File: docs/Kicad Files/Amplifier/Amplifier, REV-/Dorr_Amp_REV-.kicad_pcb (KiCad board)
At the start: 2 copper layers, 152.7 x 76.2 mm, 48 parts, among them J1 Speaker Terminals, J2 Input Terminals, J3 Power Input, Q1 2N3904, Q10 QD44H8G, Q2 QD45H8G, Q3 2N3904, Q4 2N3906, Q5 QD44H8G, Q6 2N3904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

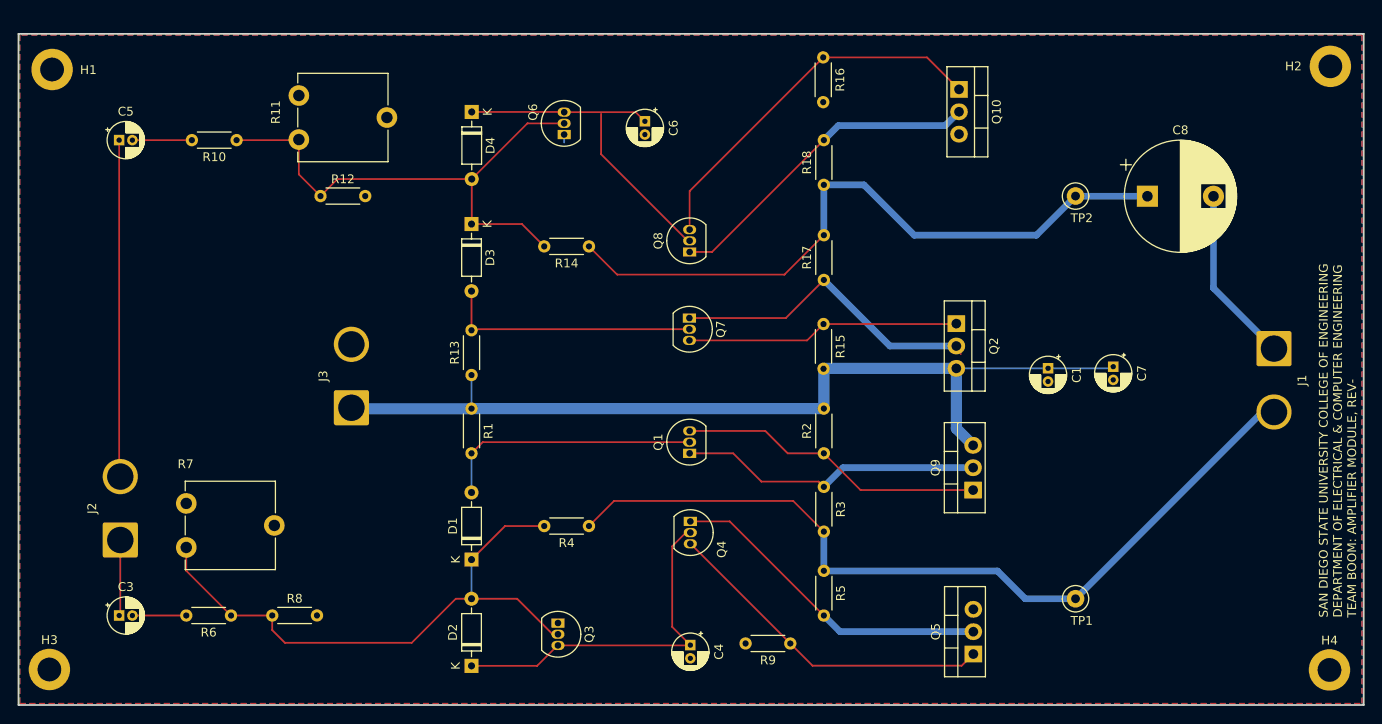
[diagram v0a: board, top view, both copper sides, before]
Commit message: Fixed all footprints
All footprints should be good. Need to double check the capacitor lead spacing with those in the lab.
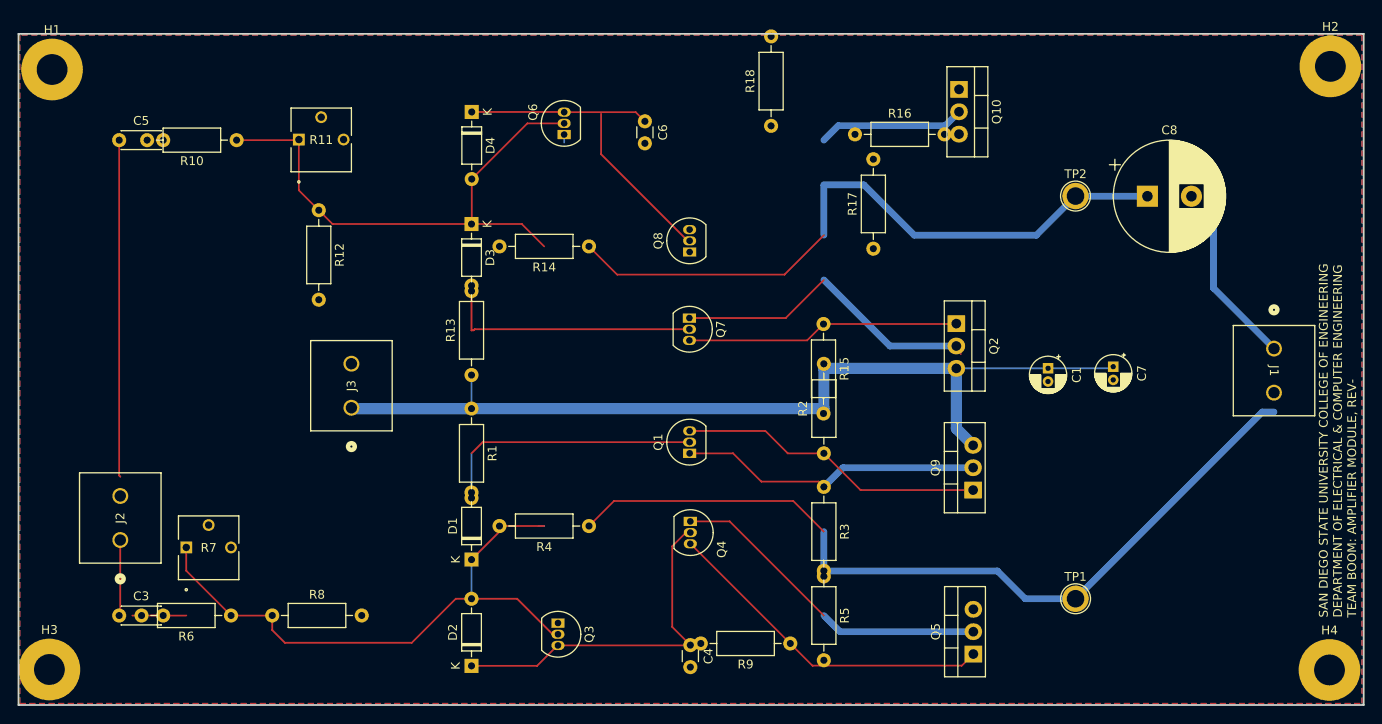
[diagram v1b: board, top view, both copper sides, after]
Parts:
- C3, C5: footprint Capacitor_THT:CP_Radial_D4.0mm_P1.50mm -> Capacitor_THT:C_Disc_D4.3mm_W1.9mm_P5.00mm
- C4, C6: footprint Capacitor_THT:CP_Radial_D4.0mm_P1.50mm -> Capacitor_THT:C_Disc_D3.0mm_W1.6mm_P2.50mm
- C8: footprint Capacitor_THT:CP_Radial_D12.5mm_P7.50mm -> Capacitor_THT:CP_Radial_D12.5mm_P5.00mm
- H1, H2, H3, H4: footprint MountingHole:MountingHole_2.7mm_M2.5_DIN965_Pad -> MountingHole:MountingHole_3.5mm_Pad
- J1: value Speaker Terminals -> Speaker; footprint Connector_Wire:SolderWire-2.5sqmm_1x02_P7.2mm_D2.4mm_OD3.6mm -> Z_Custom_Footprints:CONN_1935776_PXC
- J2, J3: footprint Connector_Wire:SolderWire-2.5sqmm_1x02_P7.2mm_D2.4mm_OD3.6mm -> Z_Custom_Footprints:CONN_1935776_PXC
- R1, R10, R12, R13, R14, R15, R16, R17, R18, R2, R3, R4, R5, R6, R8, R9: footprint Resistor_THT:R_Axial_DIN0204_L3.6mm_D1.6mm_P5.08mm_Horizontal -> Resistor_THT:R_Axial_DIN0207_L6.3mm_D2.5mm_P10.16mm_Horizontal
- R11, R7: footprint Potentiometer_THT:Potentiometer_ACP_CA9-V10_Vertical -> Z_Custom_Footprints:POT_3362P
- TP1, TP2: footprint TestPoint:TestPoint_Loop_D2.50mm_Drill1.0mm -> TestPoint:TestPoint_Plated_Hole_D2.0mm
- moved R16 9.45 mm to (133.4, 74.0), turned to 0 degrees
- moved R18 8.99 mm to (123.9, 73.1)
- moved R17 6.65 mm to (135.5, 87.0)
- moved R12 1.62 mm to (72.5, 82.7), turned to -90 degrees
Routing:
- net Net-(Q10-B): track 42.8 -> 0.00 mm
- net Net-(Q10-C): track 37.2 -> 16.7 mm
- net Net-(C5-Pad2): track 6.76 -> 0.00 mm
- net Net-(D3-K): track 60.1 -> 61.7 mm

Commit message: All footprints verified
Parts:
- C1, C7: footprint Capacitor_THT:CP_Radial_D4.0mm_P1.50mm -> Capacitor_THT:C_Rect_L7.0mm_W3.5mm_P5.00mm
- C3, C5: footprint Capacitor_THT:C_Disc_D4.3mm_W1.9mm_P5.00mm -> Capacitor_THT:CP_Radial_D5.0mm_P2.00mm
- C4, C6: footprint Capacitor_THT:C_Disc_D3.0mm_W1.6mm_P2.50mm -> Capacitor_THT:C_Disc_D5.1mm_W3.2mm_P5.00mm
- J1, J2, J3: footprint Z_Custom_Footprints:CONN_1935776_PXC -> Custom_Footprints:CONN_1935776_PXC
- R11, R7: footprint Z_Custom_Footprints:POT_3362P -> Custom_Footprints:POT_3362P

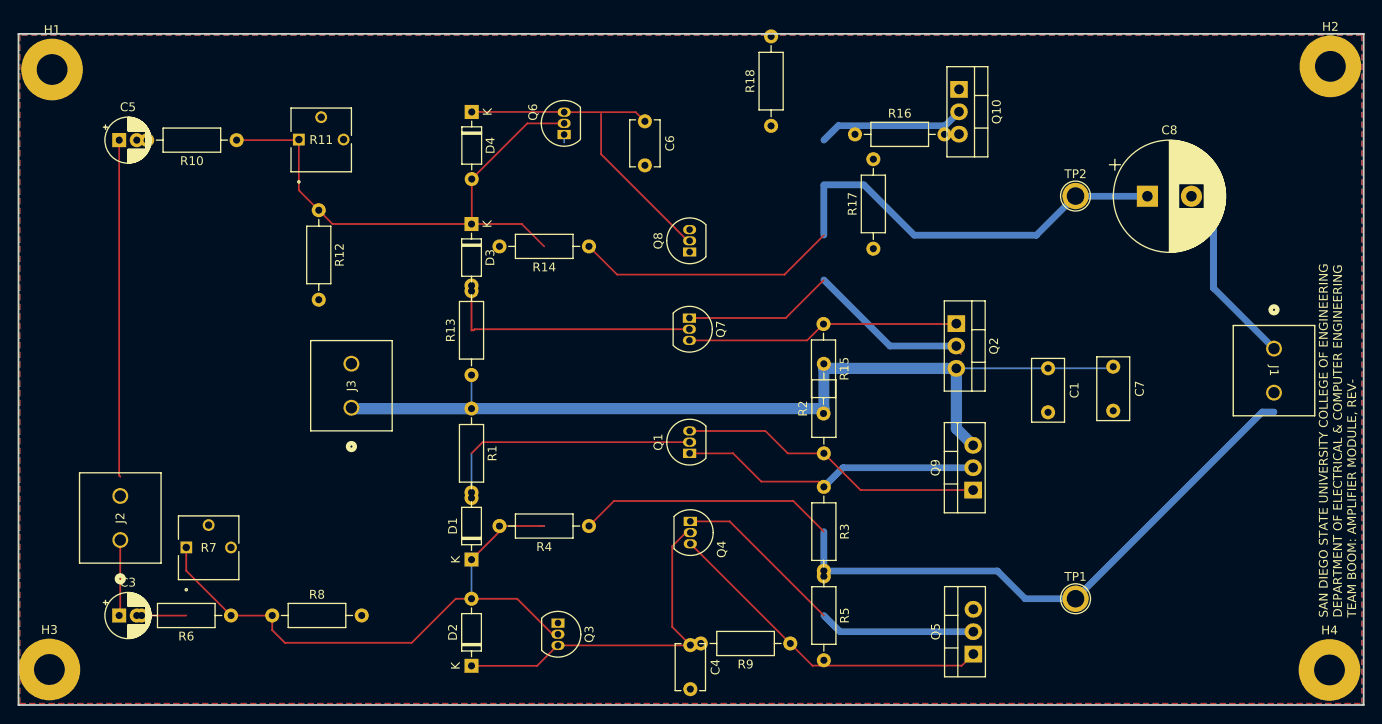
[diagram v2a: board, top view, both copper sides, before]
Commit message: removed (most) old traces
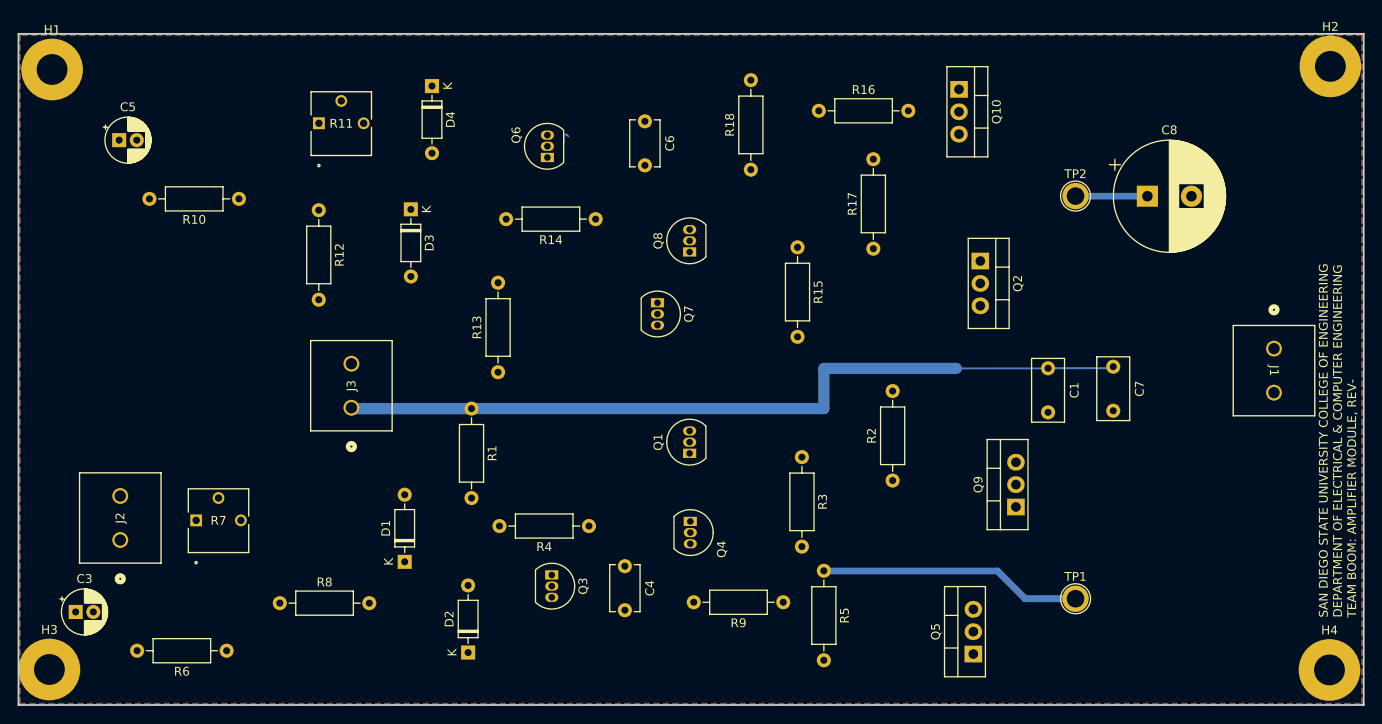
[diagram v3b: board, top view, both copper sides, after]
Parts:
- moved C4 11.6 mm to (107.3, 123.1)
- moved R15 9.20 mm to (126.9, 86.9)
- moved R2 8.40 mm to (137.7, 113.3)
- moved Q2 7.61 mm to (147.7, 88.4)
- moved D1 7.59 mm to (82.3, 122.6)
- moved D3 7.08 mm to (83.0, 82.6)
- moved R10 6.68 mm to (63.5, 81.4)
- moved Q3 5.50 mm to (99.0, 124.1)
- moved R18 5.48 mm to (121.6, 78.0)
- moved D4 5.38 mm to (85.4, 68.6)
- moved Q9 5.23 mm to (151.7, 116.3)
- moved C3 4.95 mm to (44.9, 128.3)
- moved R16 4.90 mm to (129.3, 71.4)
- moved R9 4.75 mm to (125.3, 127.2)
- moved R3 4.20 mm to (127.4, 110.7)
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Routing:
- net Net-(C8-Pad1): track 76.5 -> 8.17 mm
- net Net-(D1-K): track 67.9 -> 0.00 mm
- net Net-(J1-Pin_2): track 94.9 -> 29.9 mm
- net Net-(D3-K): track 61.7 -> 0.00 mm
- net Net-(D2-K): track 40.6 -> 0.00 mm
- net Net-(D4-K): track 39.9 -> 0.00 mm
- net Net-(J2-Pin_2): track 38.6 -> 0.00 mm
- net Net-(Q4-C): track 38.4 -> 0.00 mm
- net Net-(Q4-E): track 37.3 -> 0.00 mm
- net Net-(Q2-C): track 35.2 -> 0.00 mm
- net Net-(Q1-C): track 35.0 -> 0.00 mm
- net Net-(Q1-E): track 34.7 -> 0.00 mm
- net Net-(Q2-B): track 31.1 -> 0.00 mm
- net Net-(D1-A): track 29.7 -> 0.00 mm
- net Net-(D3-A): track 29.3 -> 0.00 mm
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
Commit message: cleaned up amp directory
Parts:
- moved R7 14.7 mm to (73.2, 119.8), turned to 90 degrees
- moved R13 5.33 mm to (96.3, 105.2)
- moved Q4 3.53 mm to (116.7, 120.9), turned to 90 degrees
- moved C6 3.50 mm to (107.6, 69.7)
- moved J1 3.35 mm to (177.6, 98.4)
- moved Q8 2.25 mm to (115.6, 85.3), turned to 180 degrees
- moved R2 1.69 mm to (137.7, 115.0)
- moved H2 1.20 mm to (186.6, 67.2)
- moved H3 1.17 mm to (43.1, 134.4)
- moved H1 0.94 mm to (43.1, 67.2)
- moved H4 0.88 mm to (186.6, 134.4)
- moved C3 0.72 mm to (45.6, 128.0)
- moved Q1 0.64 mm to (114.6, 110.9)
- moved Q7 0.54 mm to (111.0, 93.7)
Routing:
- net Net-(Q4-E): track 0.00 -> 65.7 mm
- net Net-(J1-Pin_2): track 29.9 -> 93.8 mm
- net Net-(Q1-E): track 0.00 -> 63.3 mm
- net Net-(Q10-C): track 0.00 -> 62.5 mm
- net Net-(Q2-C): track 0.00 -> 61.2 mm
- net Net-(D3-K): track 0.00 -> 60.2 mm
- net Net-(C8-Pad1): track 8.17 -> 67.2 mm
- net Net-(D1-K): track 0.00 -> 57.0 mm
- net Net-(Q10-B): track 0.00 -> 46.2 mm
- net Net-(D4-K): track 0.00 -> 46.1 mm
- net Net-(Q2-B): track 0.00 -> 43.1 mm
- net Net-(Q1-C): track 0.00 -> 41.3 mm
- net Net-(J2-Pin_2): track 0.00 -> 40.5 mm
- net Net-(Q4-C): track 0.00 -> 38.0 mm
- net Net-(D1-A): track 0.00 -> 34.9 mm
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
